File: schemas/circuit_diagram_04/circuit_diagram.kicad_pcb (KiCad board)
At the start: 2 copper layers, 71 parts, among them J1 Conn_01x02_Male, M1 PUMP_Motor, M2 Motor_DC, M3 Motor_DC, M4 Motor_DC, Q1 Q_NMOS_DGS, Q2 Q_Photo_NPN, Q3 Q_Photo_NPN, Q4 Q_Photo_NPN, Q5 Q_Photo_NPN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

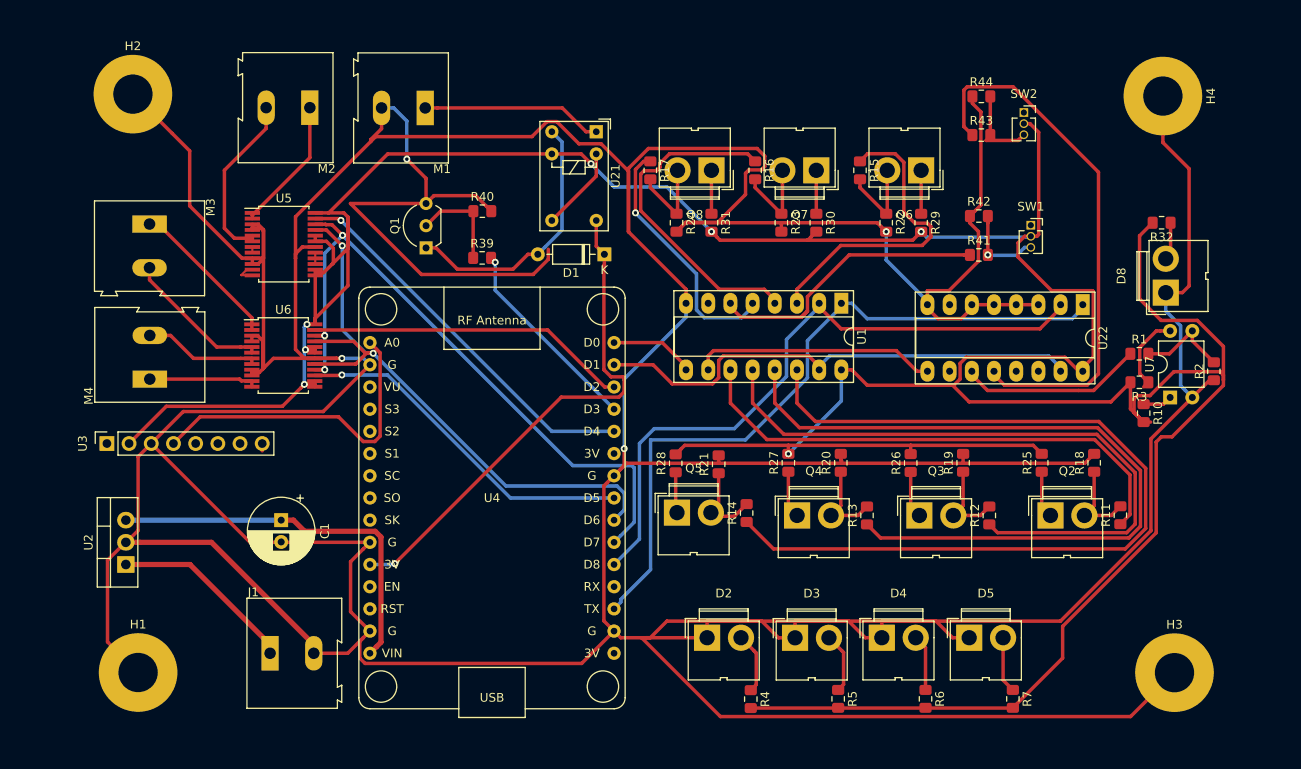
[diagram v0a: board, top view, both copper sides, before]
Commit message: PCB label added
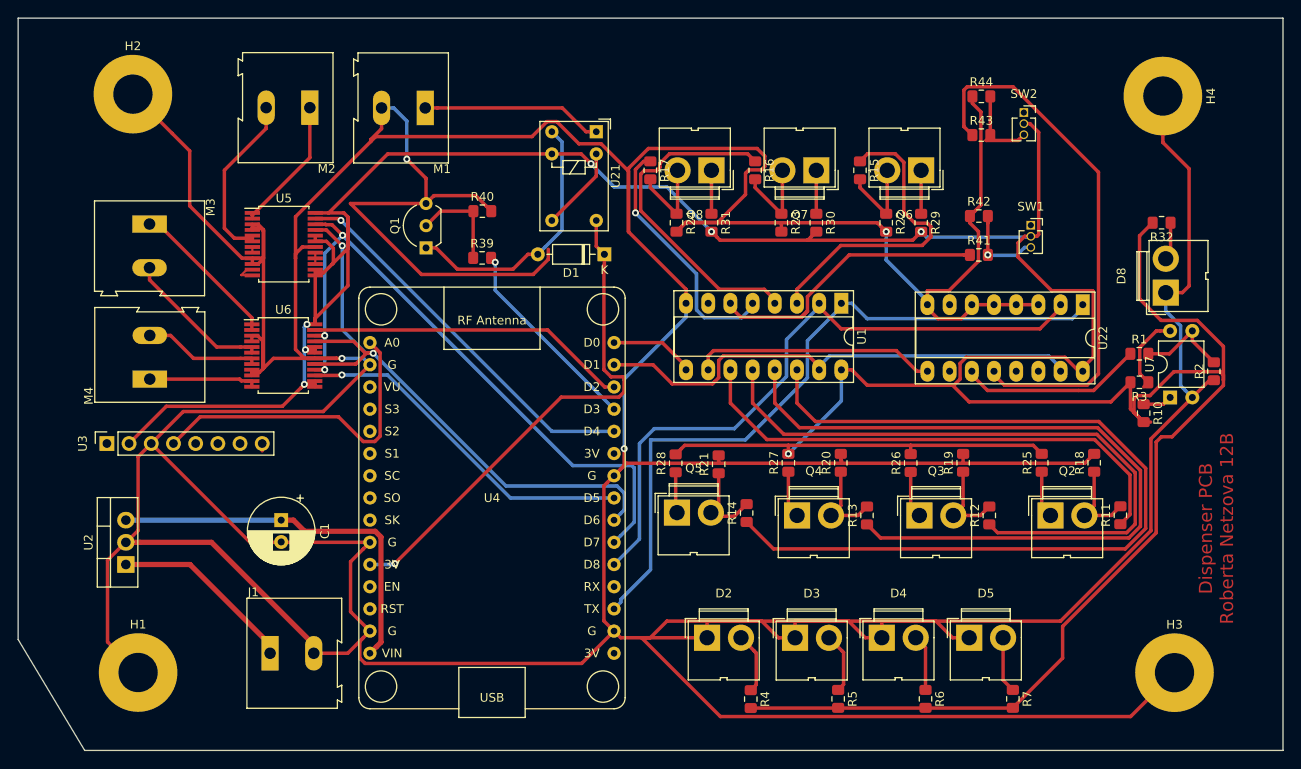
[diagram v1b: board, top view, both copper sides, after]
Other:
- board outline added: 144.8 x 83.8 mm
- board text added: "Dispenser PCB Roberta Netzova 12B"
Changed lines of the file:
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@@
   (general
     (thickness 1.6)
-    (drawings 0)
+    (drawings 6)
     (tracks 706)
     (zones 0)
@@
   )
   (setup
-    (last_trace_width 0.4)
+    (last_trace_width 0.25)
     (user_trace_width 0.4)
     (user_trace_width 0.5)
@@
     )
   )
+  (gr_text "Dispenser PCB \nRoberta Netzova 12B" (at 177.8 127 90) (layer F.Cu)
+    (effects (font (size 1.5 1.5) (thickness 0.3)))
+  )
+  (gr_line (start 40.64 68.58) (end 185.42 68.58) (layer Edge.Cuts) (width 0.15))
+  (gr_line (start 40.64 139.7) (end 40.64 68.58) (layer Edge.Cuts) (width 0.15))
+  (gr_line (start 48.26 152.4) (end 40.64 139.7) (layer Edge.Cuts) (width 0.15))
+  (gr_line (start 185.42 152.4) (end 48.26 152.4) (layer Edge.Cuts) (width 0.15))
+  (gr_line (start 185.42 68.58) (end 185.42 152.4) (layer Edge.Cuts) (width 0.15))
   (segment (start 68.58 117.2718) (end 68.58 118.11) (width 0.4) (layer F.Cu) (net 0) (status 30))
   (segment (start 106.81338 86.664) (end 101.73338 91.744) (width 0.4) (layer F.Cu) (net 0) (status 20))
